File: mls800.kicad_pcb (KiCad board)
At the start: 2 copper layers, 293.4 x 80.5 mm, 106 parts, among them CON1 BARREL_JACK, IC1 6N137, J1 USB, J10 NSJ8HC, J11 NRJ4HF-1, J2 NRJ4HF-1, J3 NSJ8HC, J4 NSJ8HC, J5 NSJ8HC, J6 NSJ8HC, J7 NSJ8HC, J8 NSJ8HC, J9 NSJ8HC, P1 CONN_02X03, P2 DIN_5, P3 DIN_5, P4 CONN_02X03, P5 CONN_02X03, SW10 SW_TACT_LED, SW11 SW_TACT_LED, SW12 SW_PUSH_RIGHT_ANGLE, SW2 SW_TACT_LED, SW3 SW_TACT_LED, SW4 SW_TACT_LED, SW5 SW_TACT_LED, SW6 SW_TACT_LED, SW7 SW_TACT_LED, SW8 SW_TACT_LED, SW9 SW_TACT_LED, U1 LM340MP-5.0/NOPB, U2 ATmega32U4-AU, U3 24LC256, U4 MCP23017, U5 AS1115, U6 ULN2803A, U7 ULN2803A, U8 LM340MP-5.0/NOPB, X1 16Mhz

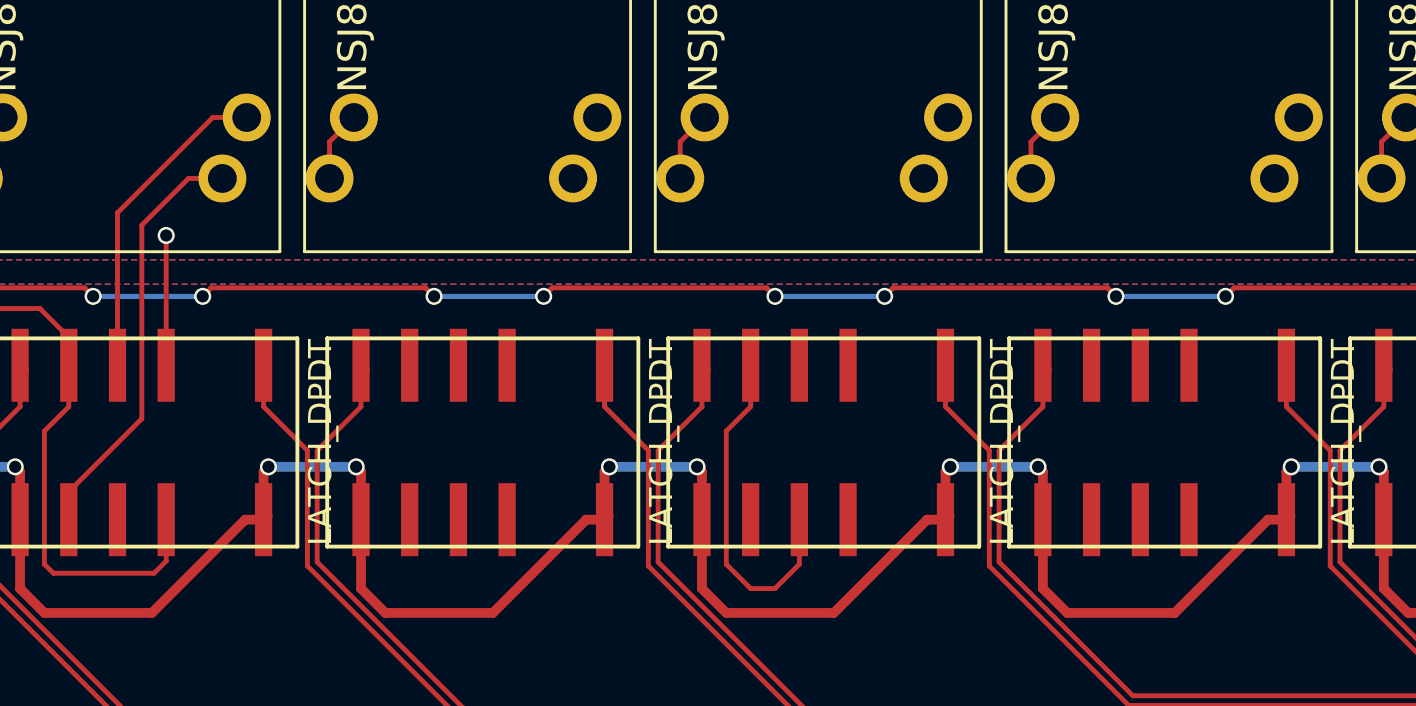
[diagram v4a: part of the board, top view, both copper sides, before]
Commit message: Routing of audio jacks
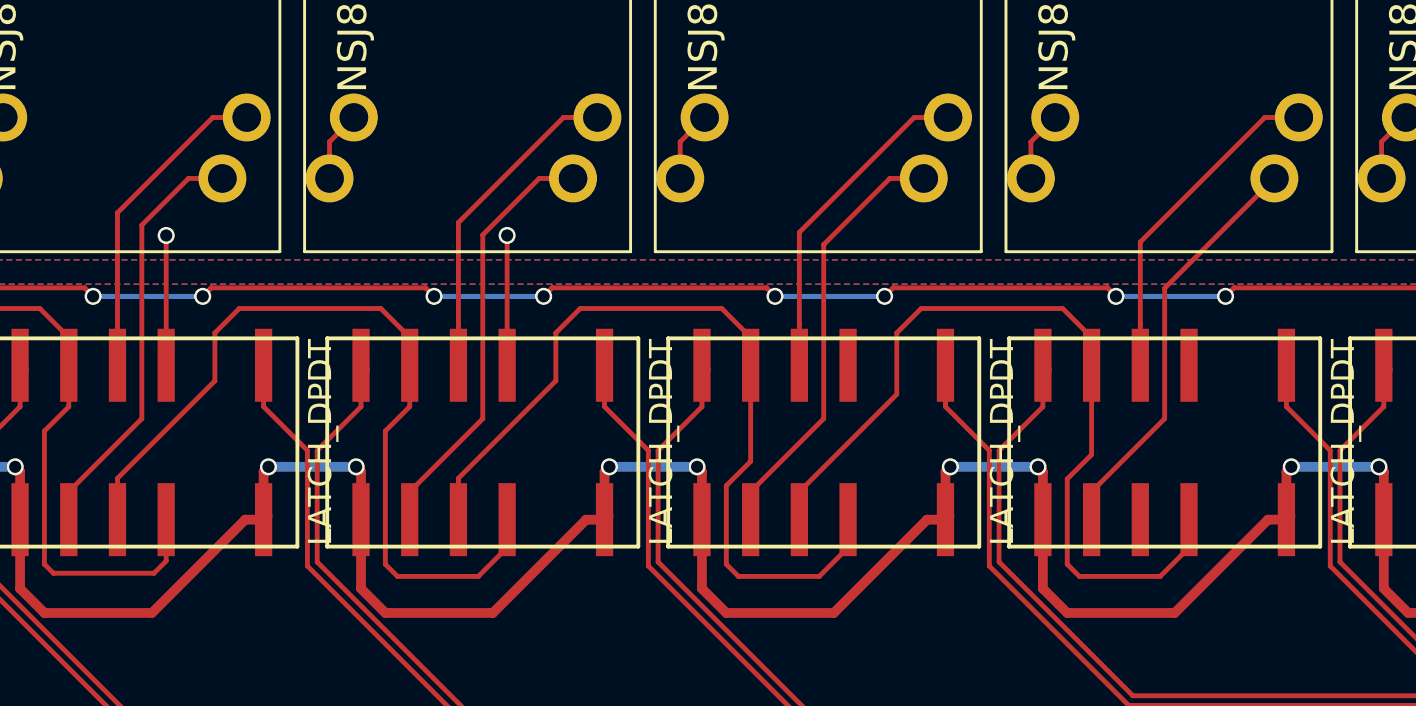
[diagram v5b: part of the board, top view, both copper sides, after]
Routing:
- net Net-(RE2-Pad9): track 0.00 -> 44.2 mm
- net Net-(RE4-Pad9): track 2.33 -> 44.2 mm
- net Net-(RE3-Pad9): track 15.8 -> 44.2 mm
- net Net-(J6-Pad5): track 1.48 -> 24.1 mm
- net Net-(J7-Pad5): track 0.00 -> 21.7 mm
- net Net-(J5-Pad5): track 1.45 -> 22.4 mm
- net Net-(J7-Pad6): track 0.00 -> 17.4 mm
- net Net-(J6-Pad6): track 0.00 -> 17.2 mm
- net Net-(J5-Pad6): track 0.00 -> 17.0 mm
- net GNDA: track 17.9 -> 24.7 mm, vias 2 -> 3
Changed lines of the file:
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@@
   (general
     (links 345)
-    (no_connects 55)
+    (no_connects 42)
     (area 29.159999 45.161999 322.630001 125.780001)
     (thickness 1.6)
     (drawings 31)
-    (tracks 1142)
+    (tracks 1204)
     (zones 0)
     (modules 106)
@@
   (segment (start 96.148 66.242) (end 96.148 64.332) (width 0.254) (layer F.Cu) (net 64))
   (segment (start 96.148 64.332) (end 97.418 63.062) (width 0.254) (layer F.Cu) (net 64))
-  (segment (start 100.33 84.035) (end 100.33 82.58) (width 0.254) (layer F.Cu) (net 65))
+  (segment (start 108.848 66.242) (end 107.080234 66.242) (width 0.254) (layer F.Cu) (net 65))
+  (segment (start 107.080234 66.242) (end 104.14 69.182234) (width 0.254) (layer F.Cu) (net 65))
+  (segment (start 104.14 69.182234) (end 104.14 78.77) (width 0.254) (layer F.Cu) (net 65))
+  (segment (start 104.14 78.77) (end 100.33 82.58) (width 0.254) (layer F.Cu) (net 65))
+  (segment (start 100.33 82.58) (end 100.33 84.035) (width 0.254) (layer F.Cu) (net 65))
+  (segment (start 110.118 63.062) (end 108.350234 63.062) (width 0.254) (layer F.Cu) (net 66))
+  (segment (start 102.87 73.826) (end 102.87 75.985) (width 0.254) (layer F.Cu) (net 66))
+  (segment (start 108.350234 63.062) (end 102.87 68.542234) (width 0.254) (layer F.Cu) (net 66))
+  (segment (start 102.87 68.542234) (end 102.87 73.826) (width 0.254) (layer F.Cu) (net 66))
   (segment (start 114.436 66.242) (end 114.436 64.332) (width 0.254) (layer F.Cu) (net 67))
   (segment (start 114.436 64.332) (end 115.706 63.062) (width 0.254) (layer F.Cu) (net 67))
+  (segment (start 127.136 66.242) (end 125.368234 66.242) (width 0.254) (layer F.Cu) (net 68))
+  (segment (start 125.368234 66.242) (end 121.92 69.690234) (width 0.254) (layer F.Cu) (net 68))
+  (segment (start 121.92 69.690234) (end 121.92 78.77) (width 0.254) (layer F.Cu) (net 68))
+  (segment (start 121.92 78.77) (end 118.11 82.58) (width 0.254) (layer F.Cu) (net 68))
+  (segment (start 118.11 82.58) (end 118.11 84.035) (width 0.254) (layer F.Cu) (net 68))
   (segment (start 118.11 84.035) (end 118.11 82.55) (width 0.254) (layer F.Cu) (net 68))
+  (segment (start 128.406 63.062) (end 126.638234 63.062) (width 0.254) (layer F.Cu) (net 69))
+  (segment (start 120.65 73.826) (end 120.65 75.985) (width 0.254) (layer F.Cu) (net 69))
+  (segment (start 126.638234 63.062) (end 120.65 69.050234) (width 0.254) (layer F.Cu) (net 69))
+  (segment (start 120.65 69.050234) (end 120.65 73.826) (width 0.254) (layer F.Cu) (net 69))
   (segment (start 132.724 66.242) (end 132.724 64.332) (width 0.254) (layer F.Cu) (net 70))
   (segment (start 132.724 64.332) (end 133.994 63.062) (width 0.254) (layer F.Cu) (net 70))
   (segment (start 134.62 63.434) (end 134.248 63.062) (width 0.254) (layer F.Cu) (net 70))
+  (segment (start 145.424 66.242) (end 139.7 71.966) (width 0.254) (layer F.Cu) (net 71))
+  (segment (start 139.7 71.966) (end 139.7 78.77) (width 0.254) (layer F.Cu) (net 71))
+  (segment (start 139.7 78.77) (end 135.89 82.58) (width 0.254) (layer F.Cu) (net 71))
+  (segment (start 135.89 82.58) (end 135.89 84.035) (width 0.254) (layer F.Cu) (net 71))
+  (segment (start 146.694 63.062) (end 144.926234 63.062) (width 0.254) (layer F.Cu) (net 72))
+  (segment (start 144.926234 63.062) (end 138.43 69.558234) (width 0.254) (layer F.Cu) (net 72))
+  (segment (start 138.43 69.558234) (end 138.43 73.826) (width 0.254) (layer F.Cu) (net 72))
+  (segment (start 138.43 73.826) (end 138.43 75.985) (width 0.254) (layer F.Cu) (net 72))
   (segment (start 151.012 66.242) (end 151.012 64.332) (width 0.254) (layer F.Cu) (net 73))
   (segment (start 151.012 64.332) (end 152.282 63.062) (width 0.254) (layer F.Cu) (net 73))
@@
   (segment (start 281.586 84.62) (end 280.035 86.171) (width 0.254) (layer F.Cu) (net 90))
   (segment (start 282.59 84.62) (end 281.586 84.62) (width 0.254) (layer F.Cu) (net 90))
+  (segment (start 105.41 75.985) (end 105.41 69.215) (width 0.254) (layer F.Cu) (net 91))
+  (via (at 105.41 69.215) (size 0.889) (drill 0.635) (layers F.Cu B.Cu) (net 91))
   (segment (start 87.63 75.985) (end 87.63 69.215) (width 0.254) (layer F.Cu) (net 91))
   (via (at 87.63 69.215) (size 0.889) (drill 0.635) (layers F.Cu B.Cu) (net 91))
@@
   (segment (start 81.045 73.025) (end 82.55 74.53) (width 0.254) (layer F.Cu) (net 118))
   (segment (start 82.55 74.53) (end 82.55 75.985) (width 0.254) (layer F.Cu) (net 118))
-  (segment (start 118.11 75.985) (end 118.11 78.144) (width 0.254) (layer F.Cu) (net 120))
-  (segment (start 118.11 78.144) (end 116.84 79.414) (width 0.254) (layer F.Cu) (net 120))
-  (segment (start 116.84 86.36) (end 118.11 87.63) (width 0.254) (layer F.Cu) (net 120))
-  (segment (start 116.84 79.414) (end 116.84 86.36) (width 0.254) (layer F.Cu) (net 120))
-  (segment (start 118.11 87.63) (end 119.38 87.63) (width 0.254) (layer F.Cu) (net 120))
-  (segment (start 119.38 87.63) (end 120.65 86.36) (width 0.254) (layer F.Cu) (net 120))
-  (segment (start 120.65 86.36) (end 120.65 84.035) (width 0.254) (layer F.Cu) (net 121))
+  (segment (start 99.06 86.36) (end 99.06 79.414) (width 0.254) (layer F.Cu) (net 119))
+  (segment (start 99.06 79.414) (end 100.33 78.144) (width 0.254) (layer F.Cu) (net 119))
+  (segment (start 100.33 78.144) (end 100.33 75.985) (width 0.254) (layer F.Cu) (net 119))
+  (segment (start 99.695 86.995) (end 99.06 86.36) (width 0.254) (layer F.Cu) (net 119))
+  (segment (start 103.905 86.995) (end 99.695 86.995) (width 0.254) (layer F.Cu) (net 119))
+  (segment (start 105.41 84.035) (end 105.41 85.49) (width 0.254) (layer F.Cu) (net 119))
+  (segment (start 105.41 85.49) (end 103.905 86.995) (width 0.254) (layer F.Cu) (net 119))
+  (segment (start 91.44 73.025) (end 98.825 73.025) (width 0.254) (layer F.Cu) (net 119))
+  (segment (start 98.825 73.025) (end 100.33 74.53) (width 0.254) (layer F.Cu) (net 119))
+  (segment (start 100.33 74.53) (end 100.33 75.985) (width 0.254) (layer F.Cu) (net 119))
+  (segment (start 90.17 74.295) (end 91.44 73.025) (width 0.254) (layer F.Cu) (net 119))
+  (segment (start 90.17 76.796) (end 90.17 74.295) (width 0.254) (layer F.Cu) (net 119))
+  (segment (start 85.09 84.035) (end 85.09 81.876) (width 0.254) (layer F.Cu) (net 119))
+  (segment (start 85.09 81.876) (end 90.17 76.796) (width 0.254) (layer F.Cu) (net 119))
+  (segment (start 102.87 84.035) (end 102.87 81.876) (width 0.254) (layer F.Cu) (net 120))
+  (segment (start 102.87 81.876) (end 107.95 76.796) (width 0.254) (layer F.Cu) (net 120))
+  (segment (start 107.95 76.796) (end 107.95 74.295) (width 0.254) (layer F.Cu) (net 120))
+  (segment (start 107.95 74.295) (end 109.22 73.025) (width 0.254) (layer F.Cu) (net 120))
+  (segment (start 118.11 74.53) (end 118.11 75.985) (width 0.254) (layer F.Cu) (net 120))
+  (segment (start 109.22 73.025) (end 116.605 73.025) (width 0.254) (layer F.Cu) (net 120))
+  (segment (start 116.605 73.025) (end 118.11 74.53) (width 0.254) (layer F.Cu) (net 120))
+  (segment (start 116.84 82.264198) (end 118.11 80.994198) (width 0.254) (layer F.Cu) (net 120))
+  (segment (start 118.11 80.994198) (end 118.11 75.985) (width 0.254) (layer F.Cu) (net 120))
+  (segment (start 116.84 86.36) (end 116.84 82.264198) (width 0.254) (layer F.Cu) (net 120))
+  (segment (start 117.475 86.995) (end 116.84 86.36) (width 0.254) (layer F.Cu) (net 120))
+  (segment (start 121.685 86.995) (end 117.475 86.995) (width 0.254) (layer F.Cu) (net 120))
+  (segment (start 123.19 84.035) (end 123.19 85.49) (width 0.254) (layer F.Cu) (net 120))
+  (segment (start 123.19 85.49) (end 121.685 86.995) (width 0.254) (layer F.Cu) (net 120))
+  (segment (start 135.89 80.645) (end 135.89 75.985) (width 0.254) (layer F.Cu) (net 121))
+  (segment (start 134.62 86.36) (end 134.62 81.915) (width 0.254) (layer F.Cu) (net 121))
+  (segment (start 134.62 81.915) (end 135.89 80.645) (width 0.254) (layer F.Cu) (net 121))
+  (segment (start 135.255 86.995) (end 134.62 86.36) (width 0.254) (layer F.Cu) (net 121))
+  (segment (start 139.465 86.995) (end 135.255 86.995) (width 0.254) (layer F.Cu) (net 121))
+  (segment (start 140.97 84.035) (end 140.97 85.49) (width 0.254) (layer F.Cu) (net 121))
+  (segment (start 140.97 85.49) (end 139.465 86.995) (width 0.254) (layer F.Cu) (net 121))
+  (segment (start 120.65 84.035) (end 120.65 82.58) (width 0.254) (layer F.Cu) (net 121))
+  (segment (start 120.65 82.58) (end 125.73 77.5) (width 0.254) (layer F.Cu) (net 121))
+  (segment (start 125.73 77.5) (end 125.73 74.295) (width 0.254) (layer F.Cu) (net 121))
+  (segment (start 125.73 74.295) (end 127 73.025) (width 0.254) (layer F.Cu) (net 121))
+  (segment (start 127 73.025) (end 134.385 73.025) (width 0.254) (layer F.Cu) (net 121))
+  (segment (start 134.385 73.025) (end 135.89 74.53) (width 0.254) (layer F.Cu) (net 121))
+  (segment (start 135.89 74.53) (end 135.89 75.985) (width 0.254) (layer F.Cu) (net 121))
   (zone (net 15) (net_name GND) (layer B.Cu) (hatch edge 0.508)
     (connect_pads (clearance 0.3))

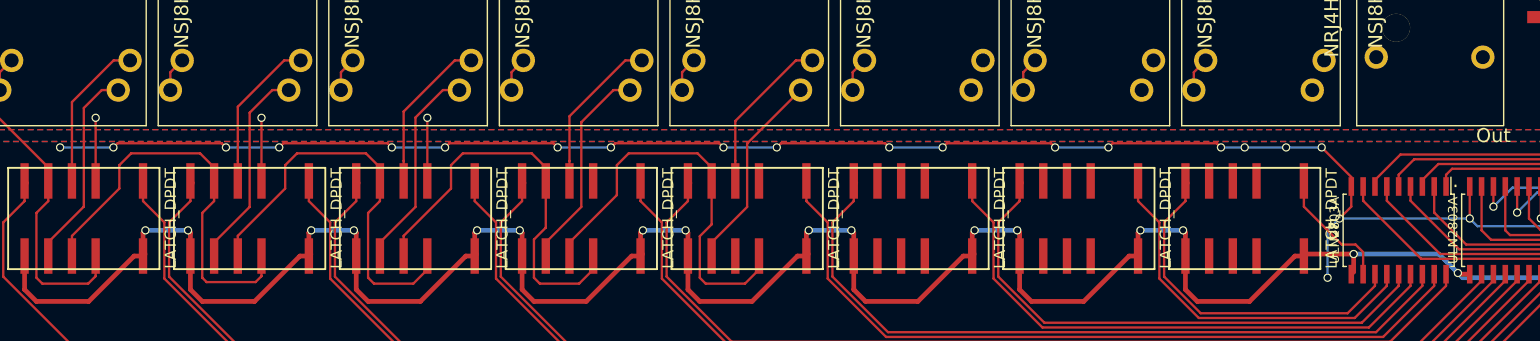
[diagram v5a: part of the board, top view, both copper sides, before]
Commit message: Jacks routing
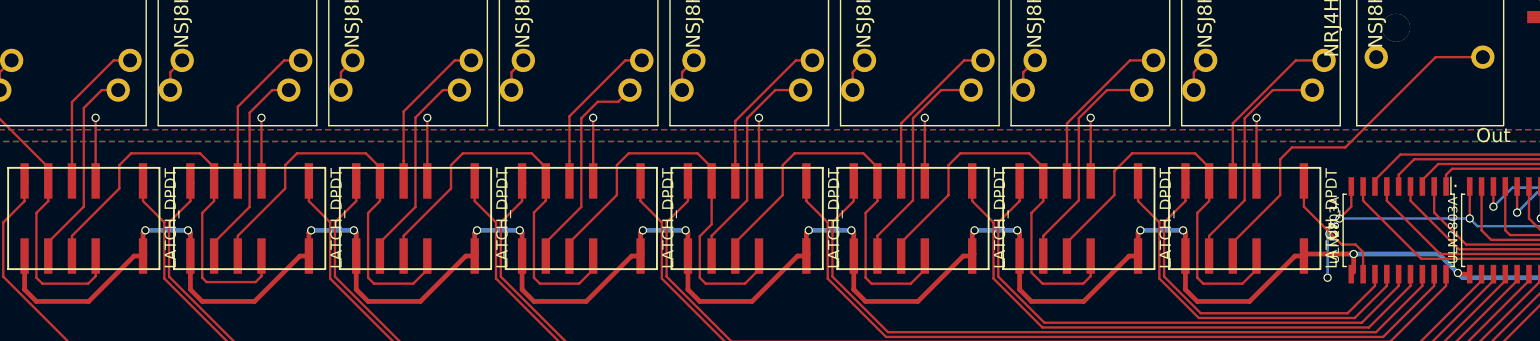
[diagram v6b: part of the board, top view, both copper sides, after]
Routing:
- net GND: track 191.1 -> 48.5 mm, vias 22 -> 4
- net Net-(RE6-Pad9): track 0.00 -> 44.3 mm
- net Net-(RE5-Pad9): track 0.00 -> 44.2 mm
- net Net-(RE7-Pad9): track 0.00 -> 43.8 mm
- net Net-(J11-Pad1): track 0.00 -> 38.7 mm
- net GNDA: track 24.7 -> 58.5 mm, vias 3 -> 8
- net Net-(J9-Pad5): track 0.00 -> 25.8 mm
- net Net-(J8-Pad5): track 0.00 -> 25.3 mm
- net Net-(J10-Pad5): track 0.00 -> 24.8 mm
- net Net-(J10-Pad6): track 0.00 -> 18.8 mm
- net Net-(J9-Pad6): track 0.00 -> 18.2 mm
- net Net-(J8-Pad6): track 0.00 -> 17.7 mm
- net Net-(J7-Pad5): track 21.7 -> 24.8 mm

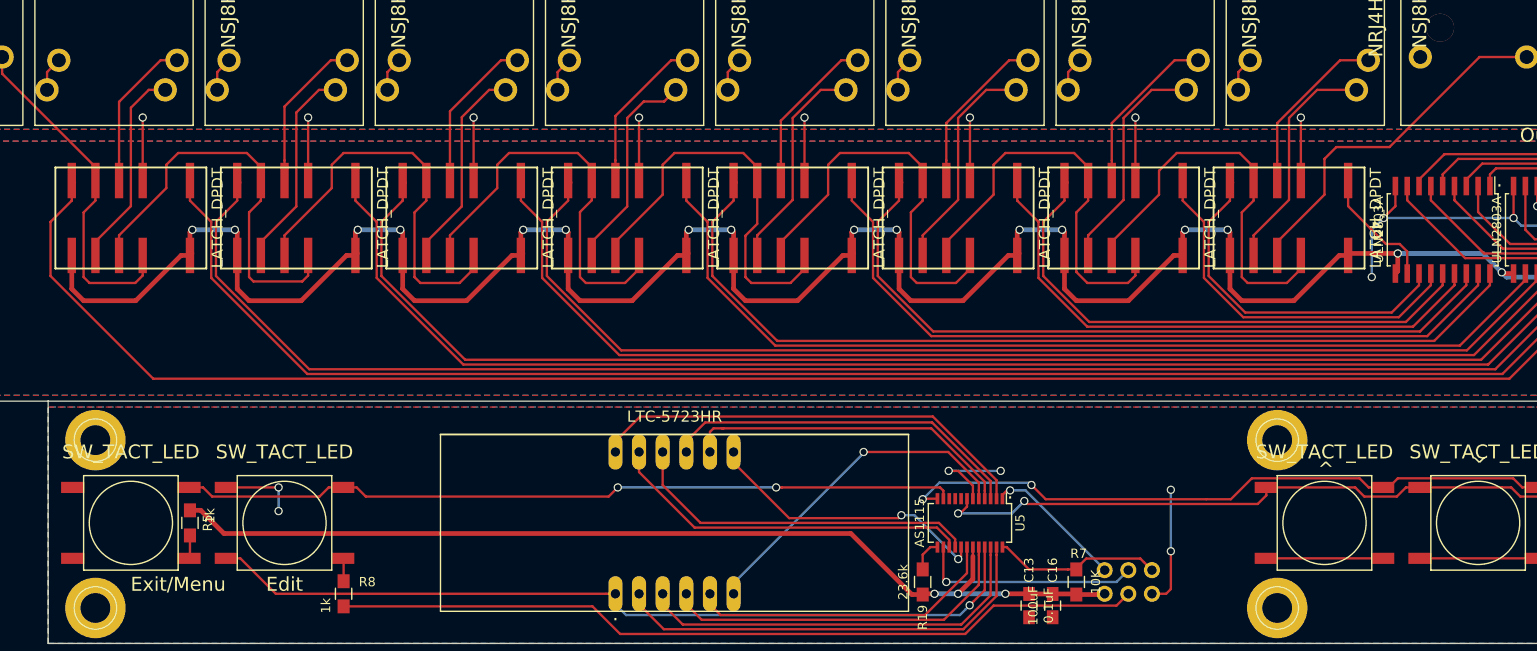
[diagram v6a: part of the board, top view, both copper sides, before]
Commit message: Optimized via positions
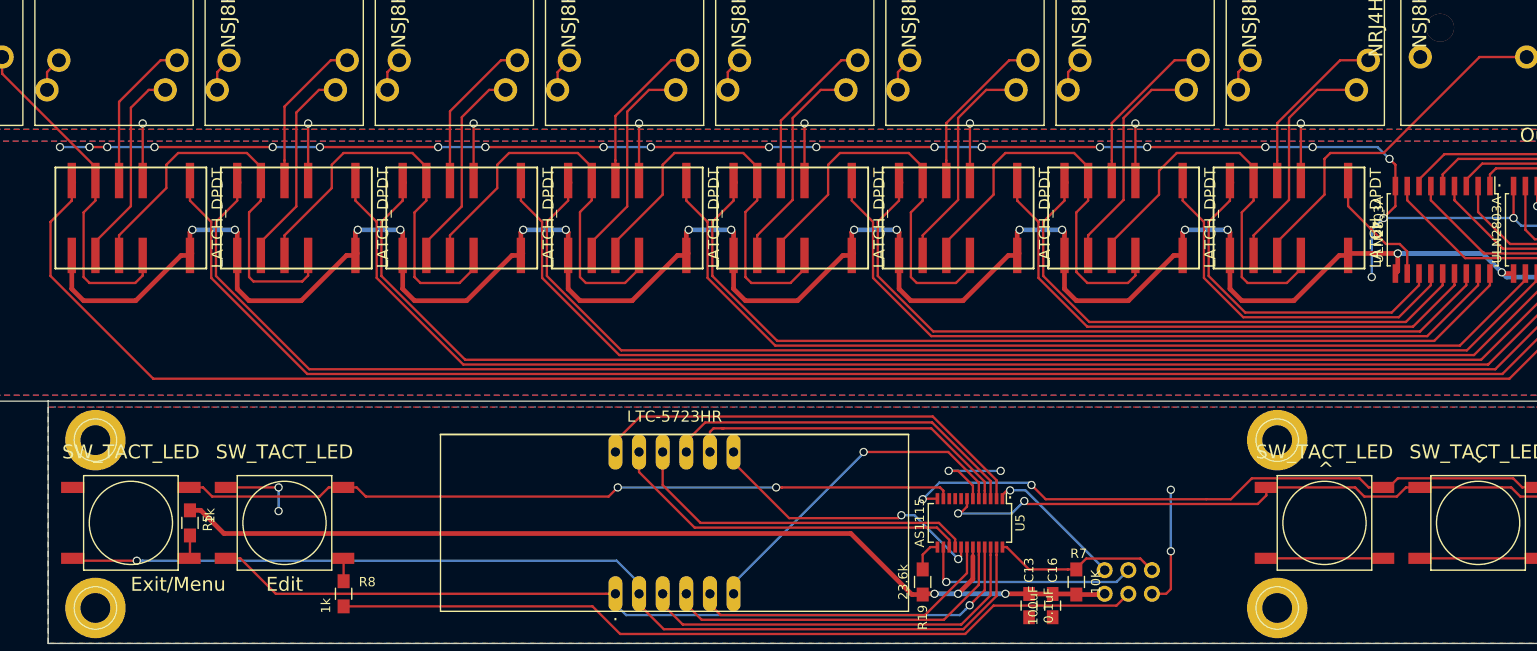
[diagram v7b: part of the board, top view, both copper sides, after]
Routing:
- net GND: track 48.5 -> 195.1 mm, vias 4 -> 23
- net /Front panel/SEGD: track 59.9 -> 123.0 mm, vias 0 -> 1
- net GNDA: track 58.5 -> 53.4 mm
